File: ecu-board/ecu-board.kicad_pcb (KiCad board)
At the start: 2 copper layers, 175 x 115 mm, 50 parts, among them J1 MicroSquirt_connector, J10 Injector connector, J11 Cockpit connector, J12 EGO connector, J13 Chrankshaft Hall connector, J14 Camshaft Hall connector, J15 Ignition 1 connector, J16 Ignition 2 connector, J17 Camera connector, J18 Wheel Hall connector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

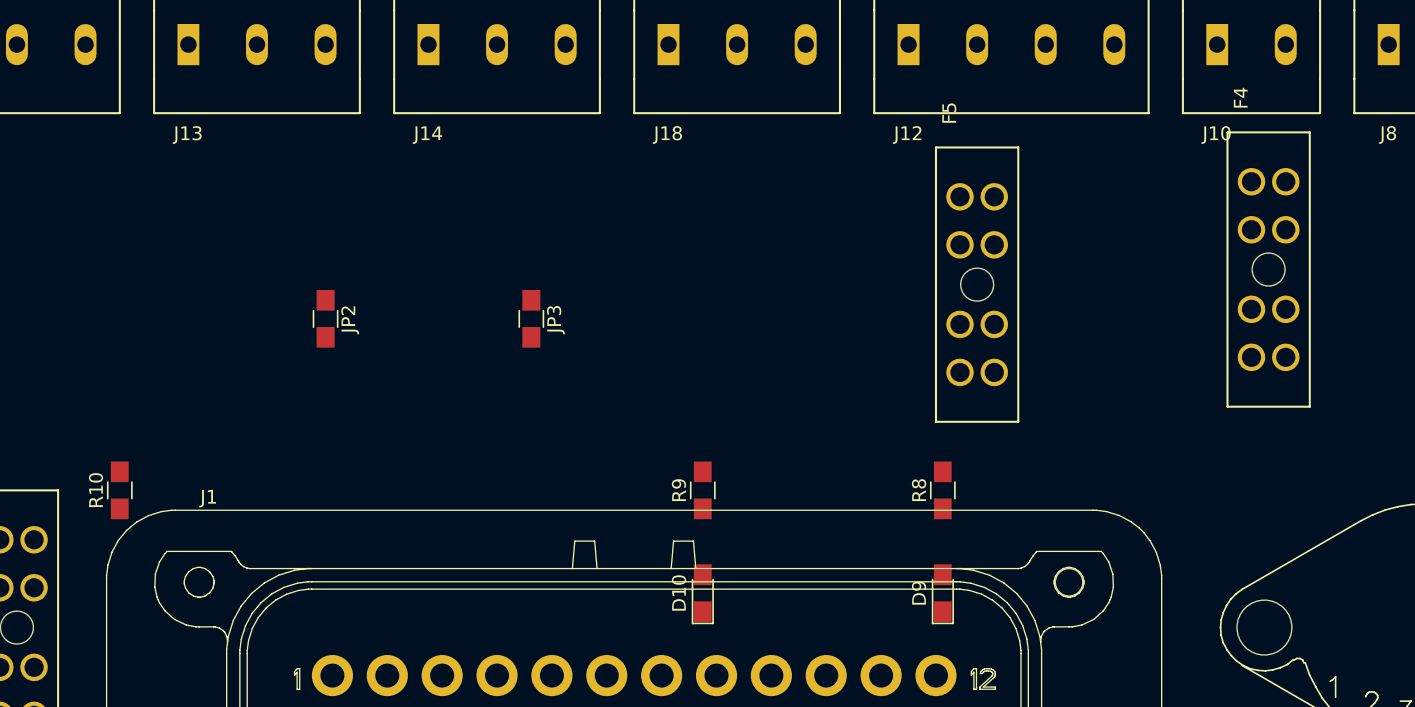
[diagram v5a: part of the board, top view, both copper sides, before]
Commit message: Rearrange some components on pcb.
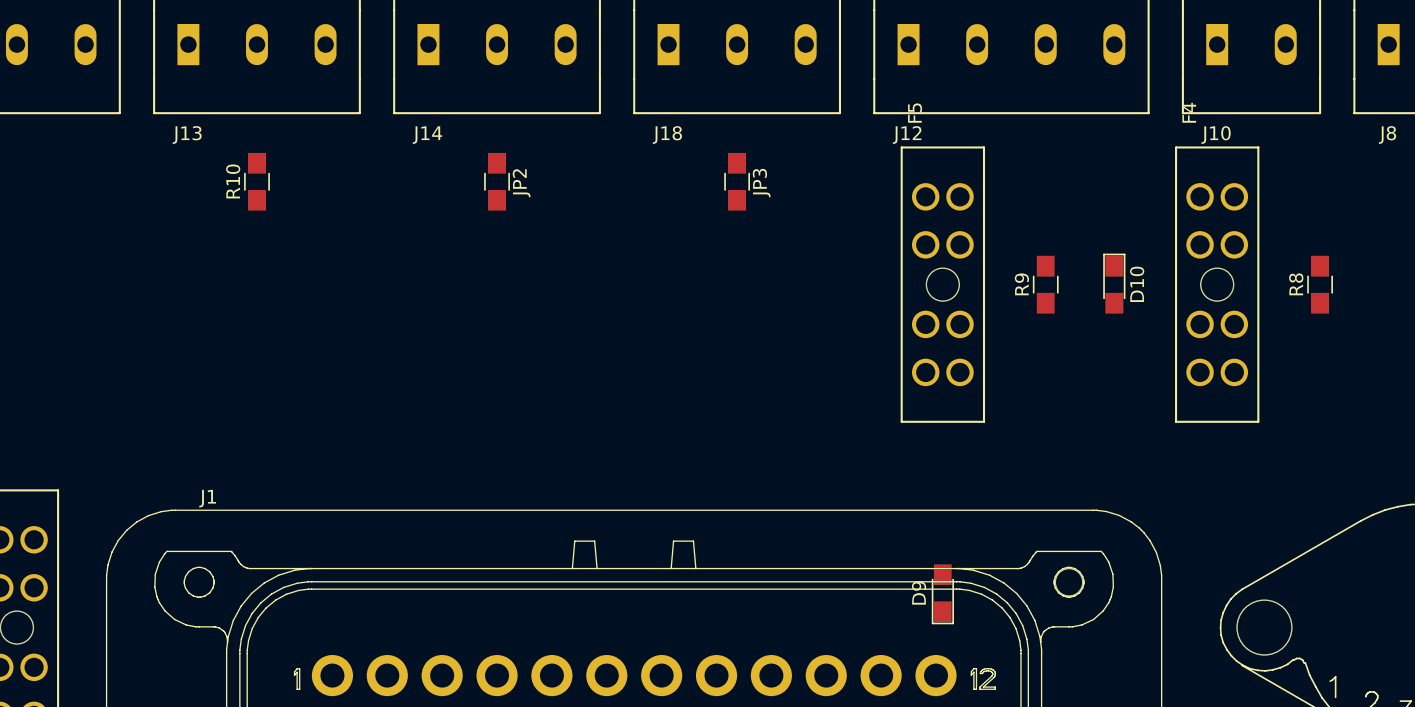
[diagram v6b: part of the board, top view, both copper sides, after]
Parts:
- moved D10 37.5 mm to (165.0, 62.5), turned to 270 degrees
- moved R8 31.3 mm to (180.0, 62.5)
- moved R9 29.2 mm to (160.0, 62.5)
- moved R10 24.6 mm to (102.5, 55.0)
- moved JP3 18.0 mm to (137.5, 55.0)
- moved JP2 16.0 mm to (120.0, 55.0)
- moved F4 3.91 mm to (172.5, 62.5)
- moved F5 2.50 mm to (152.5, 62.5)
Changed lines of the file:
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@@
     (solder_mask_min_width 0.25)
     (aux_axis_origin 0 0)
-    (visible_elements FFFFF77F)
+    (visible_elements FFFFFF7F)
     (pcbplotparams
       (layerselection 0x010fc_ffffffff)
@@
   )
   (module Resistors_SMD:R_0805_HandSoldering (layer F.Cu)
-    (at 122.5 65 270)
+    (at 137.5 55 270)
     (descr "Resistor SMD 0805, hand soldering")
     (tags "resistor 0805")
@@
   )
   (module Resistors_SMD:R_0805_HandSoldering (layer F.Cu)
-    (at 107.5 65 270)
+    (at 120 55 270)
     (descr "Resistor SMD 0805, hand soldering")
     (tags "resistor 0805")
@@
   )
   (module Resistors_SMD:R_0805_HandSoldering (layer F.Cu)
-    (at 92.5 77.5 90)
+    (at 102.5 55 90)
     (descr "Resistor SMD 0805, hand soldering")
     (tags "resistor 0805")
@@
   )
   (module Resistors_SMD:R_0805_HandSoldering (layer F.Cu)
-    (at 135 77.5 90)
+    (at 160 62.5 90)
     (descr "Resistor SMD 0805, hand soldering")
     (tags "resistor 0805")
@@
   )
   (module Resistors_SMD:R_0805_HandSoldering (layer F.Cu)
-    (at 152.5 77.5 90)
+    (at 180 62.5 90)
     (descr "Resistor SMD 0805, hand soldering")
     (tags "resistor 0805")
@@
       (effects (font (size 1 1) (thickness 0.15)))
     )
+    (fp_line (start 2.35 0.9) (end -2.35 0.9) (layer F.CrtYd) (width 0.05))
+    (fp_line (start 2.35 0.9) (end 2.35 -0.9) (layer F.CrtYd) (width 0.05))
+    (fp_line (start -2.35 -0.9) (end -2.35 0.9) (layer F.CrtYd) (width 0.05))
+    (fp_line (start -2.35 -0.9) (end 2.35 -0.9) (layer F.CrtYd) (width 0.05))
+    (fp_line (start -0.6 -0.88) (end 0.6 -0.88) (layer F.SilkS) (width 0.12))
+    (fp_line (start 0.6 0.88) (end -0.6 0.88) (layer F.SilkS) (width 0.12))
+    (fp_line (start -1 -0.62) (end 1 -0.62) (layer F.Fab) (width 0.1))
+    (fp_line (start 1 -0.62) (end 1 0.62) (layer F.Fab) (width 0.1))
+    (fp_line (start 1 0.62) (end -1 0.62) (layer F.Fab) (width 0.1))
+    (fp_line (start -1 0.62) (end -1 -0.62) (layer F.Fab) (width 0.1))
     (fp_text user %R (at 0 0 90) (layer F.Fab)
       (effects (font (size 0.5 0.5) (thickness 0.075)))
     )
-    (fp_line (start -1 0.62) (end -1 -0.62) (layer F.Fab) (width 0.1))
-    (fp_line (start 1 0.62) (end -1 0.62) (layer F.Fab) (width 0.1))
-    (fp_line (start 1 -0.62) (end 1 0.62) (layer F.Fab) (width 0.1))
-    (fp_line (start -1 -0.62) (end 1 -0.62) (layer F.Fab) (width 0.1))
-    (fp_line (start 0.6 0.88) (end -0.6 0.88) (layer F.SilkS) (width 0.12))
-    (fp_line (start -0.6 -0.88) (end 0.6 -0.88) (layer F.SilkS) (width 0.12))
-    (fp_line (start -2.35 -0.9) (end 2.35 -0.9) (layer F.CrtYd) (width 0.05))
-    (fp_line (start -2.35 -0.9) (end -2.35 0.9) (layer F.CrtYd) (width 0.05))
-    (fp_line (start 2.35 0.9) (end 2.35 -0.9) (layer F.CrtYd) (width 0.05))
-    (fp_line (start 2.35 0.9) (end -2.35 0.9) (layer F.CrtYd) (width 0.05))
+    (pad 2 smd rect (at 1.35 0 90) (size 1.5 1.3) (layers F.Cu F.Paste F.Mask)
+      (net 29 "Net-(F4-Pad2)"))
     (pad 1 smd rect (at -1.35 0 90) (size 1.5 1.3) (layers F.Cu F.Paste F.Mask)
       (net 12 "Net-(D9-Pad2)"))
-    (pad 2 smd rect (at 1.35 0 90) (size 1.5 1.3) (layers F.Cu F.Paste F.Mask)
-      (net 29 "Net-(F4-Pad2)"))
     (model ${KISYS3DMOD}/Resistors_SMD.3dshapes/R_0805.wrl
       (at (xyz 0 0 0))
@@
   )
   (module LEDs:LED_0805_HandSoldering (layer F.Cu)
-    (at 135 85 90)
+    (at 165 62.5 270)
     (descr "Resistor SMD 0805, hand soldering")
     (tags "resistor 0805")
@@
     (fp_line (start 2.35 0.9) (end -2.35 0.9) (layer F.CrtYd) (width 0.05))
     (fp_line (start -2.2 -0.75) (end -2.2 0.75) (layer F.SilkS) (width 0.12))
-    (pad 1 smd rect (at -1.35 0 90) (size 1.5 1.3) (layers F.Cu F.Paste F.Mask)
+    (pad 1 smd rect (at -1.35 0 270) (size 1.5 1.3) (layers F.Cu F.Paste F.Mask)
       (net 4 GNDS))
-    (pad 2 smd rect (at 1.35 0 90) (size 1.5 1.3) (layers F.Cu F.Paste F.Mask)
+    (pad 2 smd rect (at 1.35 0 270) (size 1.5 1.3) (layers F.Cu F.Paste F.Mask)
       (net 13 "Net-(D10-Pad2)"))
     (model ${KISYS3DMOD}/LEDs.3dshapes/LED_0805.wrl
@@
   )
   (module ecu-board-footprints:Fuseholder_ATO_Blade_Littelfuse_Pudenz_4_Pin (layer F.Cu)
-    (at 176.25 61.4 90)
+    (at 172.5 62.5 90)
     (fp_text reference F4 (at 12.5 -2 90) (layer F.SilkS)
       (effects (font (size 1 1) (thickness 0.15)))
@@
       (effects (font (size 1 1) (thickness 0.15)))
     )
+    (fp_line (start 10 -3) (end -10 -3) (layer F.CrtYd) (width 0.12))
+    (fp_line (start 10 3) (end 10 -3) (layer F.CrtYd) (width 0.12))
+    (fp_line (start -10 3) (end 10 3) (layer F.CrtYd) (width 0.12))
+    (fp_line (start -10 -3) (end -10 3) (layer F.CrtYd) (width 0.12))
+    (fp_line (start 10 3) (end -10 3) (layer F.SilkS) (width 0.15))
+    (fp_line (start 10 -3) (end 10 3) (layer F.SilkS) (width 0.15))
+    (fp_line (start -10 -3) (end 10 -3) (layer F.SilkS) (width 0.15))
     (fp_line (start -10 3) (end -10 -3) (layer F.SilkS) (width 0.15))
-    (fp_line (start -10 -3) (end 10 -3) (layer F.SilkS) (width 0.15))
-    (fp_line (start 10 -3) (end 10 3) (layer F.SilkS) (width 0.15))
-    (fp_line (start 10 3) (end -10 3) (layer F.SilkS) (width 0.15))
-    (fp_line (start -10 -3) (end -10 3) (layer F.CrtYd) (width 0.12))
-    (fp_line (start -10 3) (end 10 3) (layer F.CrtYd) (width 0.12))
-    (fp_line (start 10 3) (end 10 -3) (layer F.CrtYd) (width 0.12))
-    (fp_line (start 10 -3) (end -10 -3) (layer F.CrtYd) (width 0.12))
-    (pad "" np_thru_hole circle (at 0 0 90) (size 2.4 2.4) (drill 2.4) (layers *.Cu *.Mask))
-    (pad 1 thru_hole circle (at -2.9 1.25 90) (size 2 2) (drill 1.4) (layers *.Cu *.Mask)
+    (pad 2 thru_hole circle (at 6.4 -1.25 90) (size 2 2) (drill 1.4) (layers *.Cu *.Mask)
+      (net 29 "Net-(F4-Pad2)"))
+    (pad 2 thru_hole circle (at 2.9 1.25 90) (size 2 2) (drill 1.4) (layers *.Cu *.Mask)
+      (net 29 "Net-(F4-Pad2)"))
+    (pad 2 thru_hole circle (at 6.4 1.25 90) (size 2 2) (drill 1.4) (layers *.Cu *.Mask)
+      (net 29 "Net-(F4-Pad2)"))
+    (pad 2 thru_hole circle (at 2.9 -1.25 90) (size 2 2) (drill 1.4) (layers *.Cu *.Mask)
+      (net 29 "Net-(F4-Pad2)"))
+    (pad 1 thru_hole circle (at -6.4 -1.25 90) (size 2 2) (drill 1.4) (layers *.Cu *.Mask)
+      (net 24 /Connectors/deadmans))
+    (pad 1 thru_hole circle (at -2.9 -1.25 90) (size 2 2) (drill 1.4) (layers *.Cu *.Mask)
       (net 24 /Connectors/deadmans))
     (pad 1 thru_hole circle (at -6.4 1.25 90) (size 2 2) (drill 1.4) (layers *.Cu *.Mask)
       (net 24 /Connectors/deadmans))
-    (pad 1 thru_hole circle (at -2.9 -1.25 90) (size 2 2) (drill 1.4) (layers *.Cu *.Mask)
+    (pad 1 thru_hole circle (at -2.9 1.25 90) (size 2 2) (drill 1.4) (layers *.Cu *.Mask)
       (net 24 /Connectors/deadmans))
-    (pad 1 thru_hole circle (at -6.4 -1.25 90) (size 2 2) (drill 1.4) (layers *.Cu *.Mask)
-      (net 24 /Connectors/deadmans))
-    (pad 2 thru_hole circle (at 2.9 -1.25 90) (size 2 2) (drill 1.4) (layers *.Cu *.Mask)
-      (net 29 "Net-(F4-Pad2)"))
-    (pad 2 thru_hole circle (at 6.4 1.25 90) (size 2 2) (drill 1.4) (layers *.Cu *.Mask)
-      (net 29 "Net-(F4-Pad2)"))
-    (pad 2 thru_hole circle (at 2.9 1.25 90) (size 2 2) (drill 1.4) (layers *.Cu *.Mask)
-      (net 29 "Net-(F4-Pad2)"))
-    (pad 2 thru_hole circle (at 6.4 -1.25 90) (size 2 2) (drill 1.4) (layers *.Cu *.Mask)
-      (net 29 "Net-(F4-Pad2)"))
+    (pad "" np_thru_hole circle (at 0 0 90) (size 2.4 2.4) (drill 2.4) (layers *.Cu *.Mask))
   )
   (module ecu-board-footprints:Fuseholder_ATO_Blade_Littelfuse_Pudenz_4_Pin (layer F.Cu)
-    (at 155 62.5 90)
+    (at 152.5 62.5 90)
     (fp_text reference F5 (at 12.5 -2 90) (layer F.SilkS)
       (effects (font (size 1 1) (thickness 0.15)))

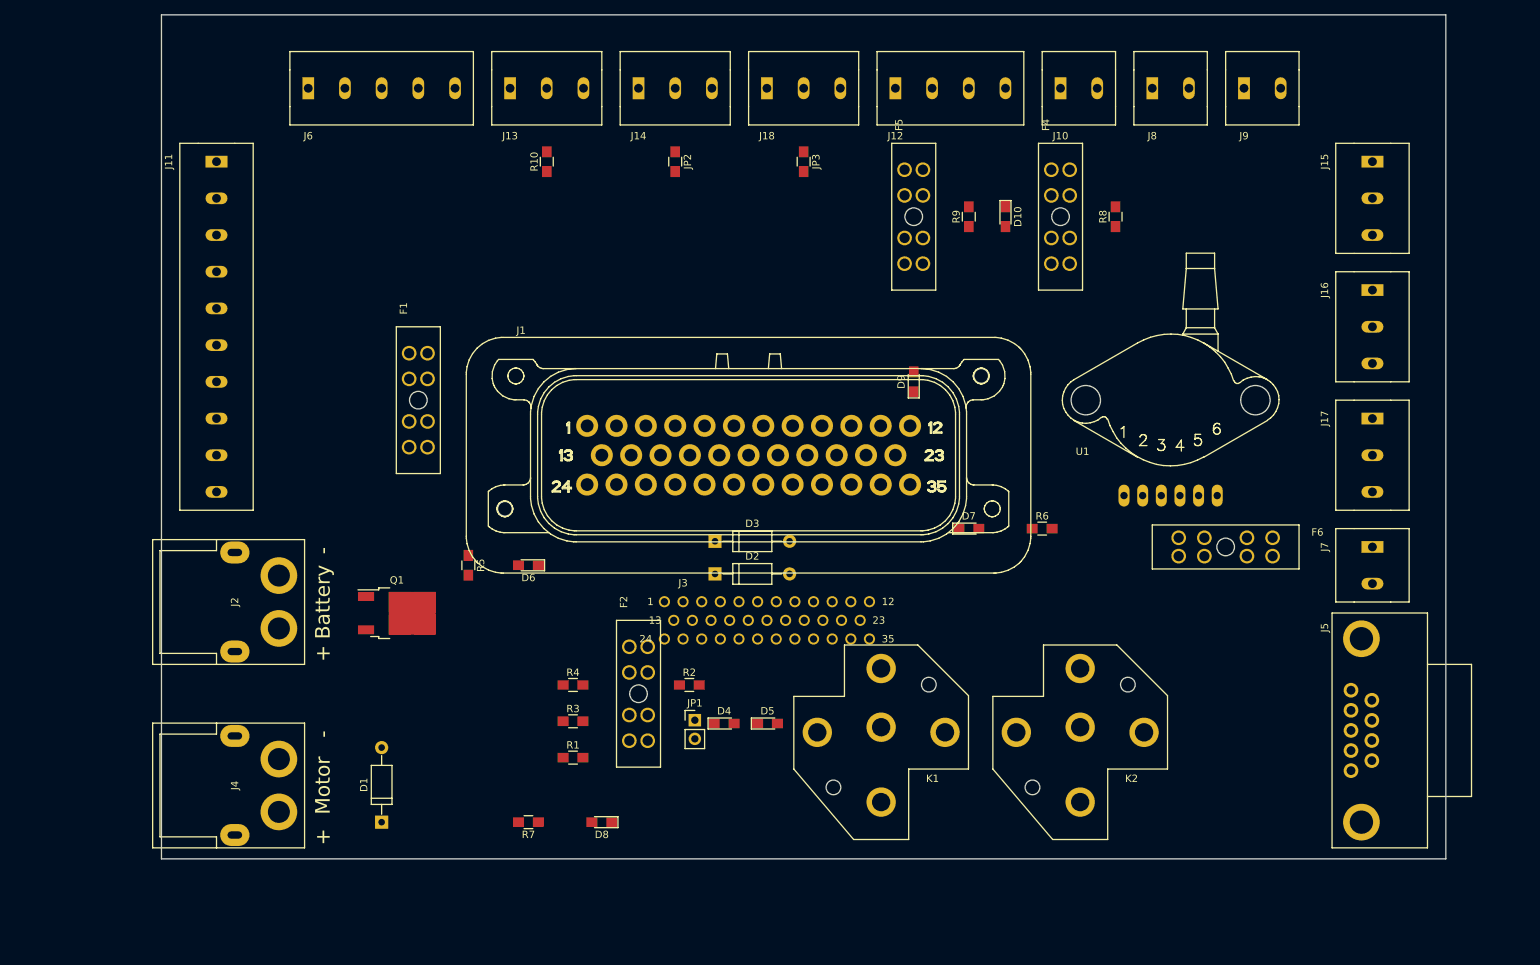
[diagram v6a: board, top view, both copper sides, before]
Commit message: Start power circuit routing.
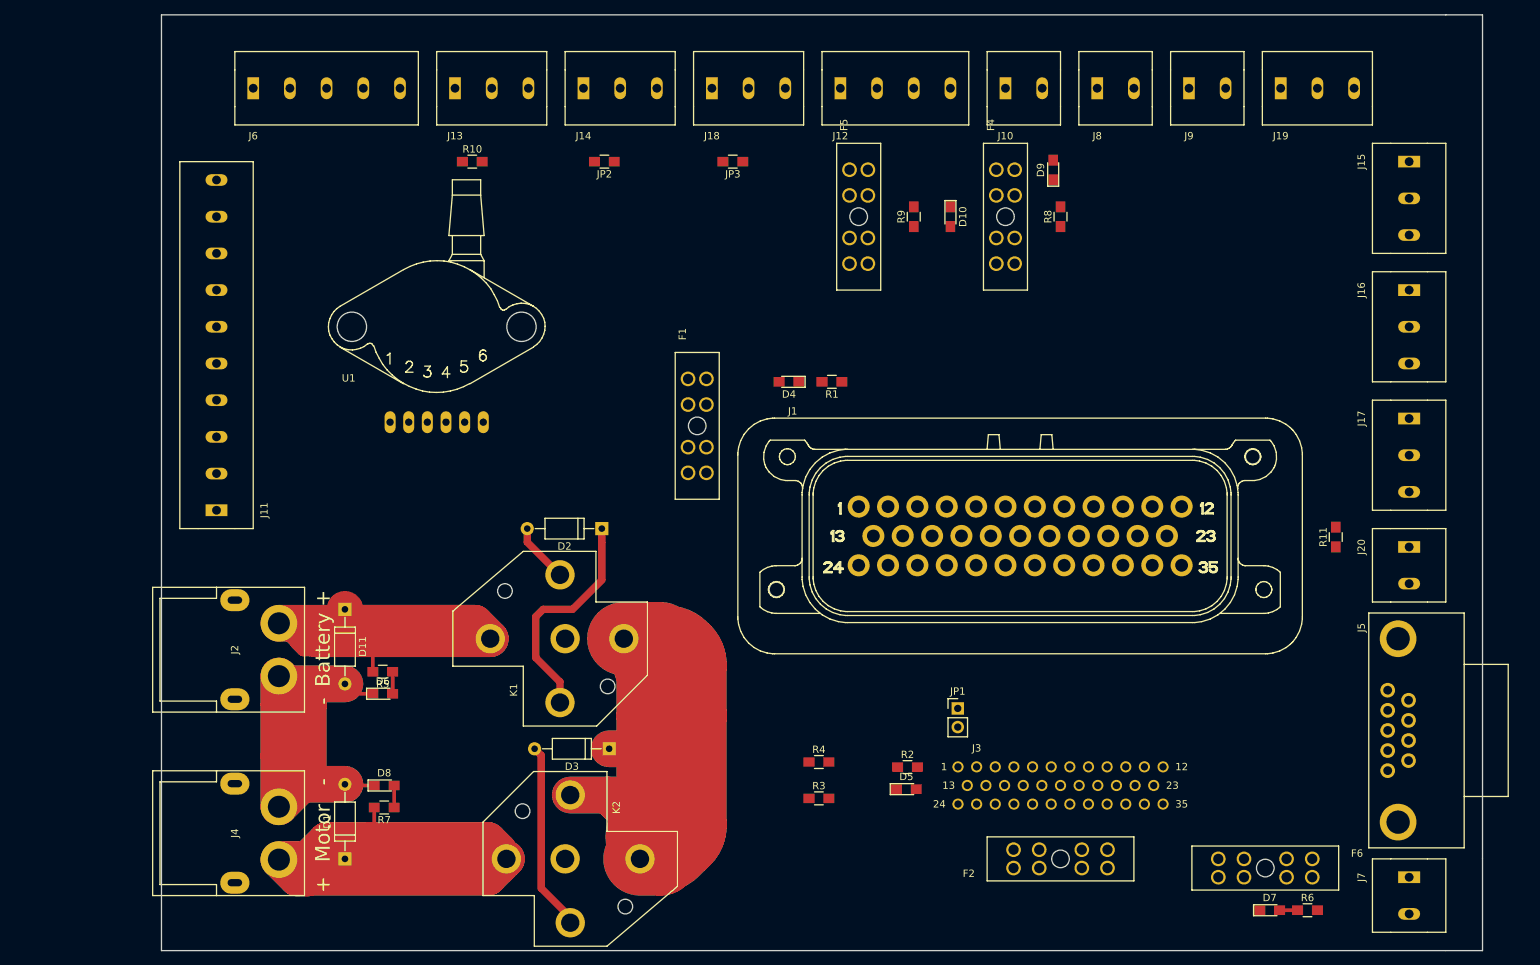
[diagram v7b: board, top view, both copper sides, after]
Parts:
- removed Q1: IPD90P03P4-04, TO_SOT_Packages_SMD:TO-252-2
- added D11: 1N5820G, Diodes_THT:D_A-405_P10.16mm_Horizontal, F.Cu at (75.0, 116.0)
- added J19: Speed sensor connector, ecu-board-footprints:Terminal_Block_3x5.00mm, F.Cu at (202.5, 45.0)
- added J20: CAN connector, ecu-board-footprints:Terminal_Block_2x5.00mm, F.Cu at (220.0, 107.5)
- added R11: 120R, Resistors_SMD:R_0805_HandSoldering, F.Cu at (210.0, 106.2)
- moved U1 100.5 mm to (87.5, 77.5)
- moved K2 72.4 mm to (105.0, 150.0), turned to 90 degrees
- moved D7 66.2 mm to (201.0, 157.0)
- moved R6 63.3 mm to (206.2, 157.0)
- moved R1 62.2 mm to (141.3, 85.0), turned to 180 degrees
- moved F2 61.7 mm to (172.5, 150.0), turned to 180 degrees
- moved J11 47.5 mm to (57.5, 102.5), turned to 90 degrees
- moved D4 47.4 mm to (135.5, 85.0), turned to 180 degrees
- moved J3 45.9 mm to (172.5, 140.0)
- moved J7 45.3 mm to (220.0, 152.5)
- moved K1 44.7 mm to (105.0, 120.0), turned to 270 degrees
- moved F6 44.1 mm to (200.4, 151.2)
- moved J1 38.6 mm to (167.0, 106.0)
- moved F1 38.2 mm to (123.0, 91.0)
- moved JP1 35.9 mm to (158.5, 129.5)
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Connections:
- net /spare_in1 renamed /speed_sensor
- J2 pad 1: Net-(J2-Pad1) -> GNDPWR
- J2 pad 2: GNDPWR -> +BATT
- J5 pad 2: /serial_RX -> /serial_TX
- J5 pad 3: /serial_TX -> /serial_RX
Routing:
- net /relay_to_start_motor: track 0.00 -> 183.7 mm
- net +BATT: track 0.00 -> 168.6 mm
- net +12V: track 0.00 -> 135.4 mm
- net GNDPWR: track 0.00 -> 125.0 mm
- net /button_to_main_relay: track 0.00 -> 31.1 mm
- net /button_to_start_motor_relay: track 0.00 -> 25.7 mm
- net GNDS: track 0.00 -> 8.15 mm
- net Net-(D8-Pad2): track 0.00 -> 3.00 mm
- net Net-(D6-Pad2): track 0.00 -> 3.00 mm
- net Net-(D7-Pad2): track 0.00 -> 2.45 mm
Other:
- board size 175 x 115 mm -> 180 x 127.5 mm
- net class Default: trace_width 0.25 -> 0.5
- net class Power added: clearance 0.2, trace_width 5, via_dia 0.8, via_drill 0.4

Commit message: Route almost everything.
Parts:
- moved J11 170.0 mm to (220.0, 52.5), turned to 270 degrees
- moved J15 162.3 mm to (60.0, 82.5), turned to 90 degrees
- moved J16 162.3 mm to (60.0, 100.0), turned to 90 degrees
- moved U1 95.5 mm to (182.5, 67.5), turned to 90 degrees
- moved D10 80.3 mm to (77.5, 68.8), turned to 90 degrees
- moved F1 76.3 mm to (192.0, 123.5), turned to 0 degrees
- moved J18 75.0 mm to (200.0, 45.0)
- moved JP3 75.0 mm to (202.8, 55.0)
- moved R9 75.0 mm to (77.5, 62.5)
- moved D4 73.8 mm to (194.0, 130.0)
- moved F5 72.7 mm to (72.5, 67.5)
- moved J12 72.5 mm to (70.0, 45.0)
- moved R3 69.0 mm to (157.2, 75.1), turned to 90 degrees
- moved R4 65.7 mm to (162.2, 75.1), turned to 90 degrees
- moved R1 65.3 mm to (188.7, 130.0)
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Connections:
- D2 pad 2: GNDS -> GNDPWR
- K1 pad 85: GNDS -> GNDPWR
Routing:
- net GNDPWR: track 125.0 -> 538.2 mm, vias 0 -> 1
- net /button_to_start_motor_relay: track 25.7 -> 342.7 mm
- net +BATT: track 168.6 -> 435.8 mm
- net /Connectors/deadmans: track 0.00 -> 238.5 mm
- net /relay_to_start_motor: track 183.7 -> 318.4 mm
- net /button_to_main_relay: track 31.1 -> 159.4 mm
- net /tachometer: track 0.00 -> 101.8 mm
- net /ignition_1: track 0.00 -> 96.5 mm
- net /ignition_2: track 0.00 -> 94.1 mm
- net /ego_signal: track 0.00 -> 92.2 mm
- net /serial_TX: track 0.00 -> 89.5 mm
- net /serial_RX: track 0.00 -> 89.1 mm
- net /crank_hall_signal: track 0.00 -> 86.3 mm, vias 0 -> 1
- net +5V: track 0.00 -> 77.9 mm, vias 0 -> 1
- net /cam_hall_signal: track 0.00 -> 75.2 mm, vias 0 -> 1
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- added copper zone on B.Cu, net +12V
- added copper zone on F.Cu, net GNDS
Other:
- outline, holes or cut-outs redrawn
- board text added: "TPS Divider"
